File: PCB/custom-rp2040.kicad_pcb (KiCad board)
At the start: 2 copper layers, 28 x 57.6 mm, 37 parts, among them J1 USB_C_Receptacle_USB2.0_16P, J2 SWD, SW1 SW_Push, U1 W25Q128JVS, U2 USBLC6-2SC6, U3 RP2040, U4 AMS1117-3.3, Y1 12MHz

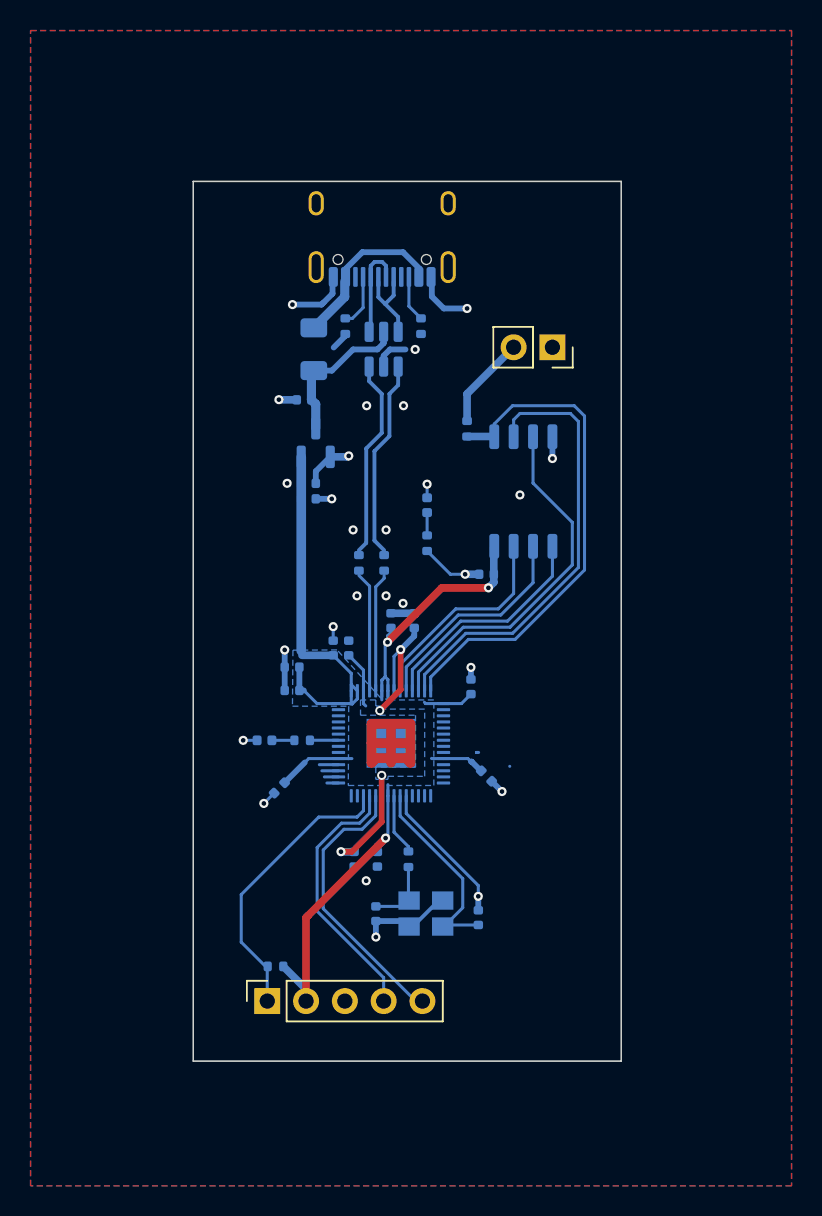
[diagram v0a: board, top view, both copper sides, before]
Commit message: Add reset and boot buttons
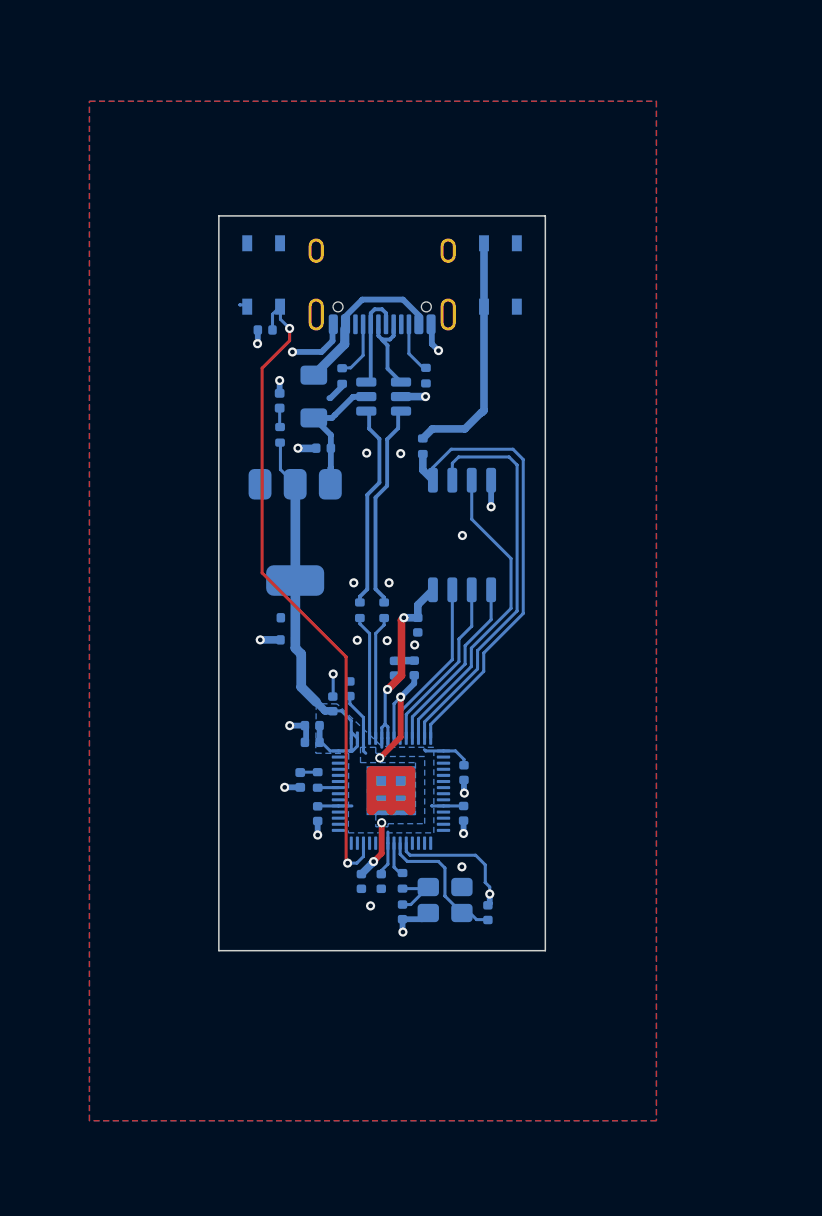
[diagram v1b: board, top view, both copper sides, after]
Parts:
- removed J2: SWD, Connector_PinSocket_2.54mm:PinSocket_1x05_P2.54mm_Vertical
- removed R2: 1k, Resistor_SMD:R_0402_1005Metric
- added C2: 100nF, Capacitor_SMD:C_0402_1005Metric, B.Cu at (97.4, 39.0)
- added SW2: SW_Push, Button_Switch_SMD:SW_SPST_PTS810, B.Cu at (97.3, 35.4)
- SW1: footprint Connector_PinSocket_2.54mm:PinSocket_1x02_P2.54mm_Vertical -> Button_Switch_SMD:SW_SPST_PTS810; moved to B.Cu
- U4: footprint Package_TO_SOT_SMD:SOT-23 -> Package_TO_SOT_SMD:SOT-223-3_TabPin2
- moved R8 12.0 mm to (98.4, 45.9)
- moved D1 11.8 mm to (98.3, 43.6)
- moved C17 9.33 mm to (98.9, 59.3)
- moved C7 8.90 mm to (98.9, 57.8), turned to 180 degrees
- moved U4 6.03 mm to (99.4, 52.2), turned to -90 degrees
- moved SW1 5.83 mm to (112.8, 35.4), turned to 90 degrees
- moved C15 5.64 mm to (110.4, 68.0), turned to -90 degrees
- moved C1 5.59 mm to (107.4, 58.3), turned to 90 degrees
- moved U1 4.92 mm to (110.3, 52.4)
- moved C14 4.05 mm to (100.5, 64.9)
- moved C8 3.66 mm to (101.8, 63.5)
- moved C9 3.65 mm to (100.5, 66.0)
- moved D2 3.49 mm to (99.7, 68.5), turned to -90 degrees
- moved C16 3.41 mm to (101.2, 46.7), turned to 180 degrees
- moved R3 3.27 mm to (102.4, 42.0), turned to 90 degrees
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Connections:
- C20 pad 1: XTAL_OUT -> /XTAL_O
- C4 pad 1: +5V -> +1V1
- C5 pad 1: +5V -> +1V1
- C6 pad 1: +5V -> +1V1
- D1 pad 1: Net-(D1-K) -> GND
- D1 pad 2: GND -> Net-(D1-A)
- D2 pad 1: Net-(D2-K) -> GND
- D2 pad 2: GND -> Net-(D2-A)
- R7 pad 1: XTAL_OUT -> /XTAL_O
- R8 pad 2: Net-(D1-K) -> Net-(D1-A)
- R9 pad 2: Net-(D2-K) -> Net-(D2-A)
- U2 pad 1: D_P -> D_USB_P
- U2 pad 3: D_N -> D_P
- U2 pad 4: D_USB_N -> D_N
- U2 pad 6: D_USB_P -> D_USB_N
- U3 pad 26: ~{RESET} -> Net-(U3-RUN)
- Y1 pad 1: XTAL_OUT -> /XTAL_O
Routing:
- net Net-(U3-RUN): track 0.00 -> 43.6 mm, vias 0 -> 2
- net +3V3: track 80.2 -> 54.4 mm, vias 5 -> 2
- net ~{RESET}: track 19.0 -> 0.00 mm
- net SWCLK: track 18.1 -> 0.00 mm
- net SWD: track 17.4 -> 0.00 mm
- net Net-(R1-Pad1): track 6.09 -> 15.7 mm
- net Net-(U3-USB_DP): track 0.00 -> 8.09 mm
- net (no net): track 7.78 -> 0.00 mm
- net GND: track 58.0 -> 51.1 mm, vias 24 -> 25
- net XTAL_OUT: track 8.58 -> 2.29 mm
- net +1V1: track 24.3 -> 19.7 mm
- net /XTAL_O: track 0.00 -> 3.89 mm
- net XTAL_IN: track 13.0 -> 9.27 mm
- net QSPI_SD0: track 15.0 -> 11.8 mm
- net QSPI_SD2: track 23.7 -> 20.5 mm
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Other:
- board size 28 x 57.6 mm -> 21.4 x 48.1 mm
